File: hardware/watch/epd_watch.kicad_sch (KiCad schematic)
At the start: 56 parts, among them J1 SWD_interface, J2 sound_connector, P1 FPC, Q1 Si1308EDL, SW1 BTN_UP, SW2 BTN_MIDDLE, SW3 BTN_DOWN, U1 nRF52832-QFxx, U2 XC6206PxxxMR, U3 TP4057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

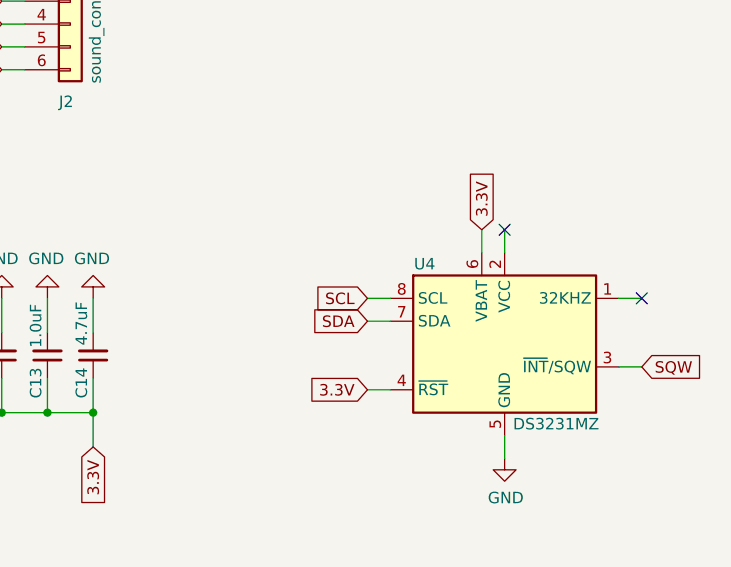
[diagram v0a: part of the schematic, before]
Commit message: didnt read datasheet well enough
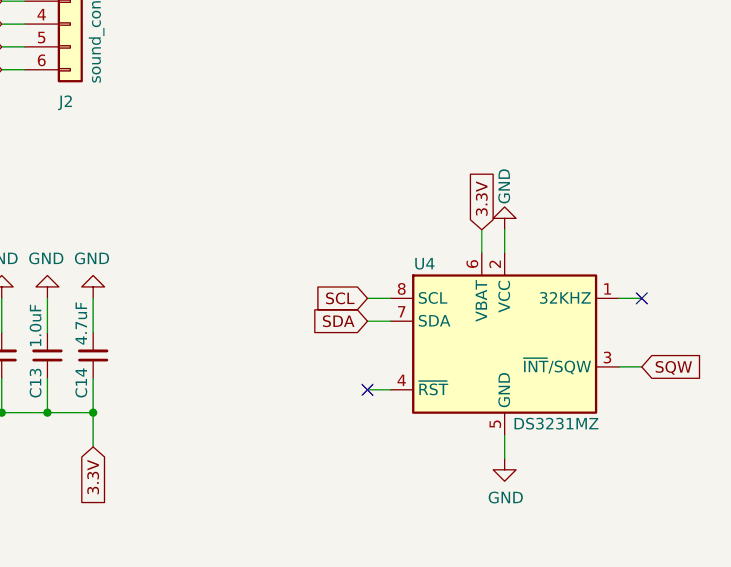
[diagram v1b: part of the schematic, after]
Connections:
- net 3.3V: no longer U4.4 (~{RST})
- net GND: now also U4.2 (VCC)
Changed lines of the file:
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@@
 	)
 	(no_connect
-		(at 252.73 123.19)
-	)
-	(no_connect
 		(at 259.08 41.91)
 	)
@@
 	)
 	(no_connect
+		(at 237.49 140.97)
+	)
+	(no_connect
 		(at 259.08 26.67)
 	)
@@
 	(wire
 		(pts
+			(xy 237.49 140.97) (xy 240.03 140.97)
+		)
+		(stroke
+			(width 0)
+			(type default)
+		)
+	)
+	(wire
+		(pts
 			(xy 26.67 92.71) (xy 35.56 92.71)
 		)
@@
 	(wire
 		(pts
-			(xy 237.49 140.97) (xy 240.03 140.97)
-		)
-		(stroke
-			(width 0)
-			(type default)
-		)
-	)
-	(wire
-		(pts
 			(xy 189.23 20.32) (xy 194.31 20.32)
 		)
@@
 		)
 	)
-	(global_label "3.3V"
-		(shape input)
-		(at 237.49 140.97 180)
-		(effects
-			(font
-				(size 1.27 1.27)
-			)
-			(justify right)
-		)
-		(property "Intersheetrefs" "${INTERSHEET_REFS}"
-			(at 237.49 140.97 0)
-			(effects
-				(font
-					(size 1.27 1.27)
-				)
-				(hide yes)
-			)
-		)
-	)
 	(global_label "RESE"
 		(shape input)
@@
 					(unit 1)
 				)
+			)
+		)
+	)
+	(symbol
+		(lib_id "EPD_watch-rescue:GND-power")
+		(at 252.73 123.19 180)
+		(unit 1)
+		(exclude_from_sim no)
+		(in_bom yes)
+		(on_board yes)
+		(dnp no)
+		(property "Reference" "#PWR015"
+			(at 252.73 116.84 0)
+			(effects
+				(font
+					(size 1.27 1.27)
+				)
+				(hide yes)
+			)
+		)
+		(property "Value" "GND"
+			(at 252.73 118.364 90)
+			(effects
+				(font
+					(size 1.27 1.27)
+				)
+			)
+		)
+		(property "Footprint" ""
+			(at 252.73 123.19 0)
+			(effects
+				(font
+					(size 1.27 1.27)
+				)
+				(hide yes)
+			)
+		)
+		(property "Datasheet" ""
+			(at 252.73 123.19 0)
+			(effects
+				(font
+					(size 1.27 1.27)
+				)
+				(hide yes)
+			)
+		)
+		(property "Description" ""
+			(at 252.73 123.19 0)
+			(effects
+				(font
+					(size 1.27 1.27)
+				)
+				(hide yes)
+			)
+		)
+		(pin "1"
+		)
+		(instances
+			(project "epd_watch"
+				(path "/ace35959-5458-48fc-8e56-dfb1f59f443c"
+					(reference "#PWR015")
+					(unit 1)
+				)

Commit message: first start at fixing battery measurement and lowering power consumption
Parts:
- removed D1, D2, D3, D4, D5: MBR0530, Diode_SMD:D_SOD-123, symbol Diode:MBR0530
- removed J2: sound_connector, Connector_PinSocket_1.27mm:PinSocket_1x06_P1.27mm_Vertical, symbol Connector_Generic:Conn_01x06
- added BZ1: FUET-4020, epd_watch:FUET-4020, symbol Device:Buzzer
- added C27, C28: 4.7uF, Capacitor_SMD:C_0402_1005Metric, symbol Device:C_Small
- added D4, D5, D6: 1N5819WS, Diode_SMD:D_SOD-323, symbol Diode:1N5819WS
- added J2: GPIO, epd_watch:pogo_conn, symbol Connector_Generic:Conn_01x04
- added Q2: AO3401A, Package_TO_SOT_SMD:SOT-23, symbol Transistor_FET:AO3401A
- added Q3: Si1308EDL, Package_TO_SOT_SMD:SOT-323_SC-70, symbol Transistor_FET:Si1308EDL
- added R2, R7, R8: 10K, Resistor_SMD:R_0402_1005Metric, symbol Device:R_Small
- added U5: LM66100DCK, Package_TO_SOT_SMD:SOT-363_SC-70-6, symbol Power_Management:LM66100DCK
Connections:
- net 3.3V: now also C21.1, P1.15 (VDDIO), P1.16 (VCI), J2.1 (Pin_1)
- net BTN_DOWN: now also U1.7 (P0.05/AIN3); no longer U1.9 (P0.07)
- net BTN_MIDDLE: now also U1.8 (P0.06); no longer U1.10 (P0.08)
- net BTN_UP: now also U1.9 (P0.07); no longer U1.11 (NFC1/P0.09)
- net BUSY: now also U1.37 (P0.25); no longer U1.38 (P0.26)
- net CS: now also U1.40 (P0.28/AIN4); no longer U1.41 (P0.29/AIN5)
- net DC: now also U1.39 (P0.27); no longer U1.40 (P0.28/AIN4)
- net GND: now also BZ1.2 (-), C27.1, C28.2, D5.1 (K), J2.4 (Pin_4), R8.2, U5.2 (GND)
- net MOSI: now also U1.42 (P0.30/AIN6); no longer U1.43 (P0.31/AIN7)
- net PREVGH: now also D6.1 (K)
- net PREVGL: now also D4.2 (A)
- net RES: now also U1.38 (P0.26); no longer U1.39 (P0.27)
- net SCK: now also U1.41 (P0.29/AIN5); no longer U1.42 (P0.30/AIN6)
- net SQW: now also U1.10 (P0.08); no longer U1.12 (NFC2/P0.10)
- net VBUS: now also C28.1, R2.1, U5.1 (VIN)
- net at U2.3 (VI): now also C27.2, Q2.3 (D), U5.6 (VOUT)
- net VBAT: now reaches BT1.1 (+), C15.2, U3.3 (BAT)
- net VBAT: now also Q2.2 (S), Q3.3 (D), U5.3 (~{CE})
- net BAT_LVL: now reaches U1.28 (P0.23)
- net BAT_LVL: now also R7.2, R8.1
- net BAT_LVL_EN: now reaches U1.29 (P0.24)
- net BAT_LVL_EN: now also Q3.1 (G)
- net at C8.1: now also D4.1 (K), D5.2 (A)
- net at C8.2, L5.2, Q1.3 (D): now also D6.2 (A)
- removed net EPD_3.3V: C21.1, P1.15 (VDDIO), P1.16 (VCI), U1.37 (P0.25)
- net SND_0 renamed BUZZER
- net BUZZER: now also BZ1.1 (+)
- net SND_1: no longer names the net of U1.21 (P0.18/SWO)
- net SND_2 renamed GPIO_0
- net GPIO_0: now also J2.2 (Pin_2)
- net SND_3 renamed GPIO_1
- net GPIO_1: now also J2.3 (Pin_3)
- new net: Q2.1 (G), R2.2, U5.5 (ST)
- new net: Q3.2 (S), R7.1
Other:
- note added: "TODO: look further into power consumption"
- note added: "TODO: update LCSC values"
- moved on the sheet: AE1, BT1, C1, C15, C2, C25, C26, C3, C4, C5, C6, J1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

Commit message: finalized V2.4
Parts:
- removed J2: GPIO, epd_watch:pogo_conn, symbol Connector_Generic:Conn_01x04
- added J2: GPIO, epd_watch:gpio_conn, symbol Connector_Generic:Conn_01x06
- BZ1: LCSC (none) -> C391027
- C13, C15, C17, C19, C21, C22: LCSC C7472948 -> C1518208
- C27, C28: LCSC C7472948 -> C2858031
- C4: value 1.0uF -> 1.0uF/50V; LCSC C7472948 -> C1518208
- D4, D5, D6: LCSC (none) -> C191023
- L5: LCSC C426327 -> C426327
- P1: LCSC C2856821 -> C2856821
- Q2: LCSC (none) -> C15127
- R1: LCSC C25744 -> C25744
- R4: LCSC C423162 -> C423162
- R6: LCSC C423196 -> C423196
- U5: LCSC (none) -> C2869734
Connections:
- net 3.3V: now also J2.1 (Pin_1)
- net BUZZER: now also U1.19 (P0.16); no longer U1.20 (P0.17)
- net GND: now also Q3.2 (S), J2.6 (Pin_6); no longer R8.2
- net GPIO_0: now also U1.20 (P0.17), J2.2 (Pin_2); no longer U1.22 (P0.19)
- net GPIO_1: now also U1.21 (P0.18/SWO), J2.3 (Pin_3); no longer U1.23 (P0.20)
- net VBAT: now also R7.1; no longer Q3.3 (D)
- new net: Q3.3 (D), R8.2
- new net GPIO_2: J2.4 (Pin_4), U1.22 (P0.19)
- new net GPIO_3: J2.5 (Pin_5), U1.23 (P0.20)
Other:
- note removed: "TODO: look further into power consumption"
- note removed: "TODO: update LCSC values"
- moved on the sheet: BT1, C15, C28, Q3, R5, R7, R8, U3
